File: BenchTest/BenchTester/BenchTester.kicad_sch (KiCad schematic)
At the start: 20 parts, among them J1 Conn_01x01_Socket, J2 Conn_01x01_Socket, J3 Conn_01x01_Socket, J5 Conn_01x01_Socket, J6 Conn_01x01_Socket, J7 Conn_01x01_Socket, J8 Conn_01x01_Socket, J9 Conn_01x01_Socket, Q1 Q_NMOS_Depletion_DGS, Q2 Q_NMOS_Depletion_DGS, Q3 Q_NMOS_Depletion_DGS, Q4 Q_NMOS_Depletion_DGS

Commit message: WIP for Zenn motor controller
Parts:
- added D1, D2, D3, D4: D_KAA, symbol Device:D_KAA
- added H1, H2, H3, H4: MountingHole, MountingHole:MountingHole_5.3mm_M5, symbol Mechanical:MountingHole
- added J4: Conn_01x02_Socket, Connector_PinHeader_2.54mm:PinHeader_1x02_P2.54mm_Vertical, symbol Connector:Conn_01x02_Socket
- R1, R3, R7, R8: value R -> 100k; footprint (none) -> Resistor_SMD:R_0402_1005Metric
- R2, R4, R5, R6: footprint (none) -> Resistor_SMD:R_0402_1005Metric
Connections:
- net DBUS: now also D1.1 (K), D4.1 (K)
- net GND: now also J4.2 (Pin_2)
- net Motor0: now also D1.2 (A), D1.3 (A), D2.1 (K)
- net Motor1: now also D3.1 (K), D4.2 (A), D4.3 (A)
- net SBUS: now also D2.2 (A), D2.3 (A), D3.2 (A), D3.3 (A)
- net Vdrive: now also J4.1 (Pin_1)

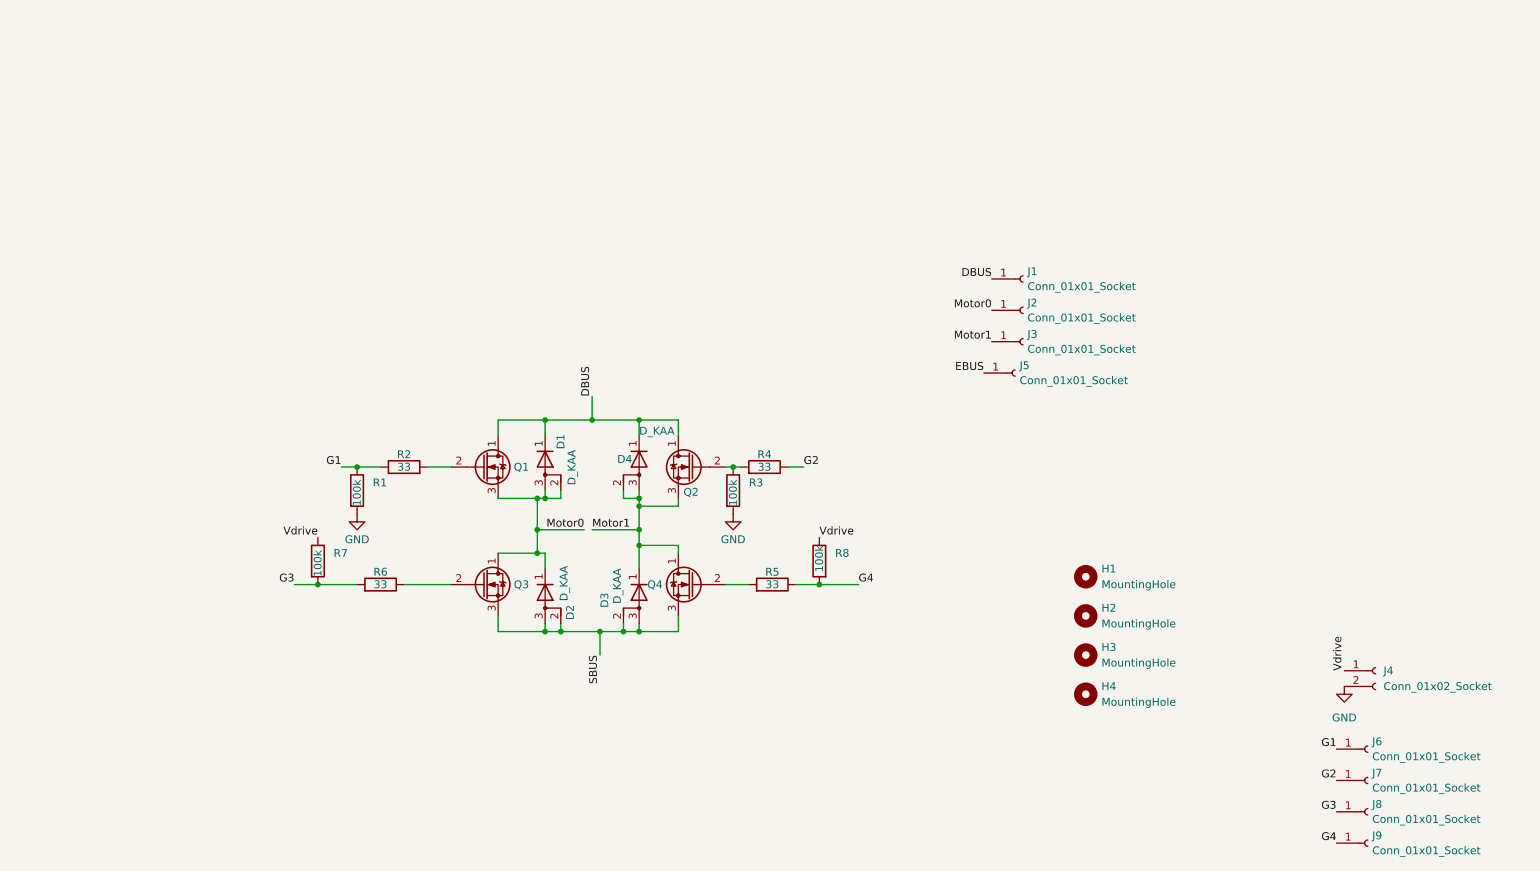
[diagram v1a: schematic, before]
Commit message: WIP - Diode / major parts assignment.
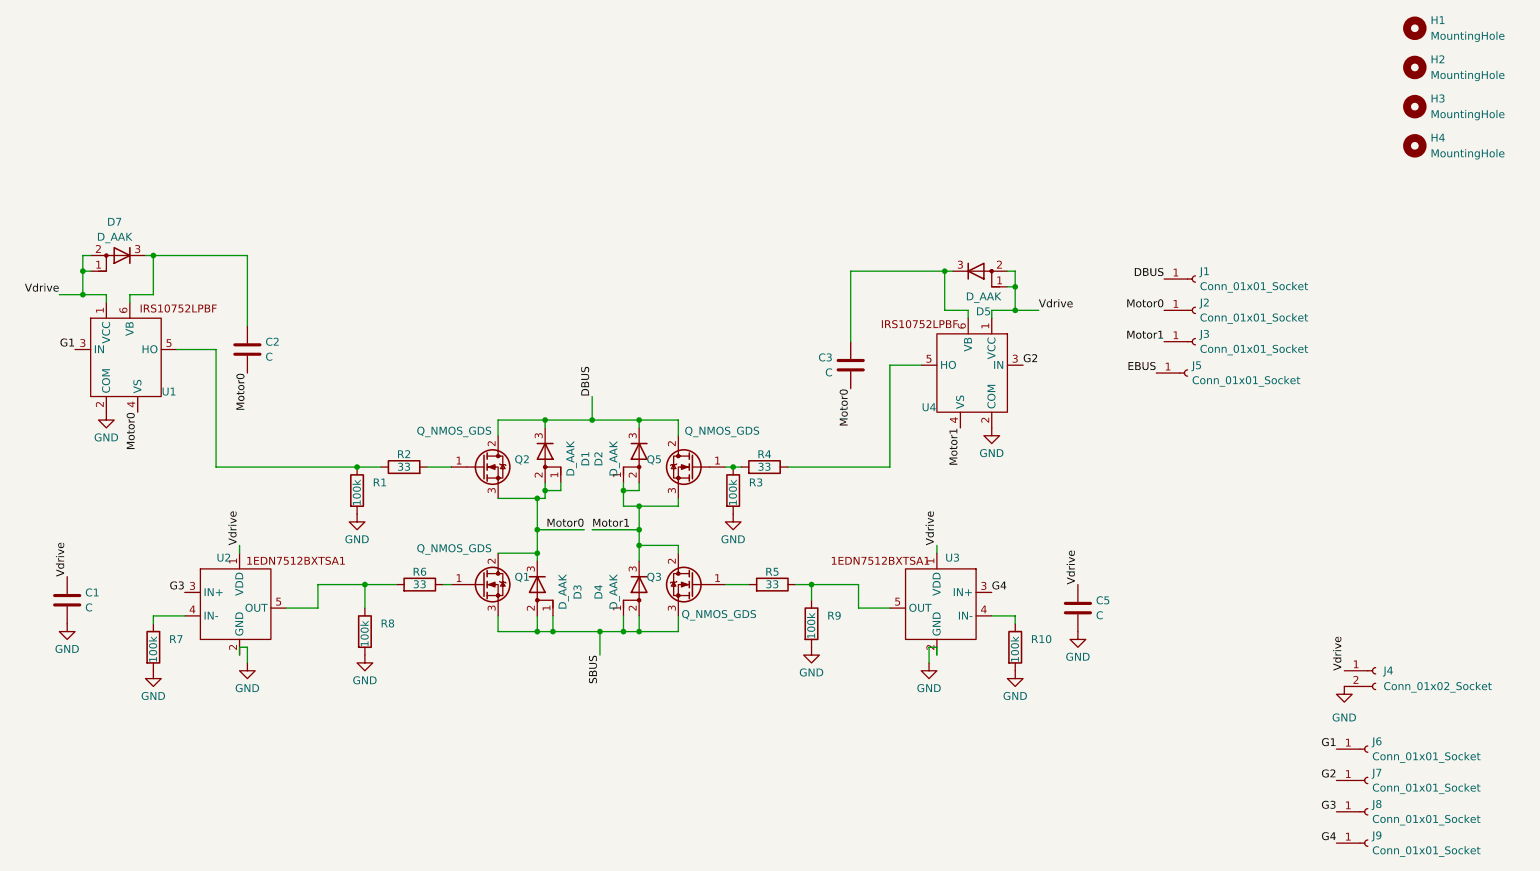
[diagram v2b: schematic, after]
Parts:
- removed D1, D2, D3, D4: D_KAA, symbol Device:D_KAA
- removed Q1, Q2, Q3, Q4: Q_NMOS_Depletion_DGS, symbol Device:Q_NMOS_Depletion_DGS
- added C1, C2, C3, C5: C, Capacitor_SMD:C_0805_2012Metric, symbol Device:C
- added D1, D2, D3, D4, D5, D7: D_AAK, Library:TO-252-2_SBR20M150D1Q, symbol Device:D_AAK
- added Q1, Q2, Q3, Q5: Q_NMOS_GDS, Package_TO_SOT_THT:TO-220-3_Vertical, symbol Device:Q_NMOS_GDS
- added R10, R9: 100k, Resistor_SMD:R_0402_1005Metric, symbol Device:R
- added U1, U4: ~, Package_TO_SOT_SMD:SOT-23-6_Handsoldering, symbol New_Library:IRS10752LPBF
- added U2, U3: ~, Package_TO_SOT_SMD:SC-74A-5_1.55x2.9mm_P0.95mm, symbol New_Library:1EDN7512BXTSA1
- H1, H2, H3: footprint MountingHole:MountingHole_5.3mm_M5 -> MountingHole:MountingHole_3.2mm_M3
- H4: footprint MountingHole:MountingHole_5.3mm_M5 -> MountingHole:MountingHole_3.2mm_M3_Pad
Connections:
- net DBUS: now also D1.3 (K), D2.3 (K), Q2.2 (D), Q5.2 (D)
- net G1: now also U1.3 (IN); no longer R1.1, R2.1
- net G2: now also U4.3 (IN); no longer R4.1
- net G3: now also U2.3 (IN+); no longer R6.2, R7.2
- net G4: now also U3.3 (IN+); no longer R5.1, R8.2
- net GND: now also R7.2, R8.2, C1.2, C5.2, R10.2, R9.2, U1.2 (COM), U2.2 (GND), U3.2 (GND), U4.2 (COM)
- net Motor0: now also C2.2, C3.2, D1.1 (A), D1.2 (A), D3.3 (K), Q1.2 (D), Q2.3 (S), U1.4 (VS)
- net Motor1: now also D2.1 (A), D2.2 (A), D4.3 (K), Q3.2 (D), Q5.3 (S), U4.4 (VS)
- net SBUS: now also D3.1 (A), D3.2 (A), D4.1 (A), D4.2 (A), Q1.3 (S), Q3.3 (S)
- net Vdrive: now also C1.1, C5.1, D5.1 (A), D5.2 (A), D7.1 (A), D7.2 (A), U1.1 (VCC), U2.1 (VDD), U3.1 (VDD), U4.1 (VCC); no longer R7.1, R8.1
- net at R2.2: now also Q2.1 (G)
- net at R3.1, R4.2: now also Q5.1 (G)
- net at R6.1: now also Q1.1 (G)
- net at R5.2: now also Q3.1 (G)
- new net: R6.2, R8.1, U2.5 (OUT)
- new net: R1.1, R2.1, U1.5 (HO)
- new net: C2.1, D7.3 (K), U1.6 (VB)
- new net: C3.1, D5.3 (K), U4.6 (VB)
- new net: R4.1, U4.5 (HO)
- new net: R10.1, U3.4 (IN-)
- new net: R5.1, R9.1, U3.5 (OUT)
- new net: R7.1, U2.4 (IN-)
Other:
- moved on the sheet: H1, H2, H3, H4, J1, J2, J3, J5, R6

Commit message: Initial Placement
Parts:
- H4: footprint MountingHole:MountingHole_3.2mm_M3_Pad -> MountingHole:MountingHole_3.2mm_M3
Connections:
- net EBUS is gone; now on net SBUS: J5.1 (Pin_1)
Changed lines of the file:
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@@
 	(label "Motor0"
 		(at 71.12 72.39 270)
-		(fields_autoplaced yes)
 		(effects
 			(font
@@
 	(label "G4"
 		(at 191.77 107.95 0)
-		(fields_autoplaced yes)
 		(effects
 			(font
@@
 	(label "DBUS"
 		(at 219.71 57.15 180)
-		(fields_autoplaced yes)
 		(effects
 			(font
@@
 	(label "Motor0"
 		(at 125.73 97.79 180)
-		(fields_autoplaced yes)
 		(effects
 			(font
@@
 	(label "Vdrive"
 		(at 69.85 100.33 90)
-		(fields_autoplaced yes)
 		(effects
 			(font
@@
 	(label "G1"
 		(at 43.18 68.58 180)
-		(fields_autoplaced yes)
 		(effects
 			(font
@@
 	(label "G2"
 		(at 247.65 138.43 180)
-		(fields_autoplaced yes)
 		(effects
 			(font
@@
 	(label "DBUS"
 		(at 127 76.2 90)
-		(fields_autoplaced yes)
 		(effects
 			(font
@@
 	(label "Motor1"
 		(at 127 97.79 0)
-		(fields_autoplaced yes)
 		(effects
 			(font
@@
 	(label "Motor0"
 		(at 168.91 74.93 270)
-		(fields_autoplaced yes)
 		(effects
 			(font
@@
 		)
 	)
-	(label "EBUS"
+	(label "SBUS"
 		(at 218.44 72.39 180)
-		(fields_autoplaced yes)
 		(effects
 			(font
@@
 	(label "Vdrive"
 		(at 248.92 120.65 90)
-		(fields_autoplaced yes)
 		(effects
 			(font
@@
 	(label "Vdrive"
 		(at 40.64 59.69 180)
-		(fields_autoplaced yes)
 		(effects
 			(font
@@
 	(label "Motor0"
 		(at 219.71 62.23 180)
-		(fields_autoplaced yes)
 		(effects
 			(font
@@
 	(label "SBUS"
 		(at 128.27 118.11 270)
-		(fields_autoplaced yes)
 		(effects
 			(font
@@
 	(label "Motor1"
 		(at 186.69 81.28 270)
-		(fields_autoplaced yes)
 		(effects
 			(font
@@
 	(label "G3"
 		(at 60.96 107.95 180)
-		(fields_autoplaced yes)
 		(effects
 			(font
@@
 	(label "G2"
 		(at 196.85 71.12 0)
-		(fields_autoplaced yes)
 		(effects
 			(font
@@
 	(label "Vdrive"
 		(at 205.74 106.68 90)
-		(fields_autoplaced yes)
 		(effects
 			(font
@@
 	(label "Motor0"
 		(at 53.34 78.74 270)
-		(fields_autoplaced yes)
 		(effects
 			(font
@@
 	(label "Vdrive"
 		(at 41.91 105.41 90)
-		(fields_autoplaced yes)
 		(effects
 			(font
@@
 	(label "Vdrive"
 		(at 199.39 62.23 0)
-		(fields_autoplaced yes)
 		(effects
 			(font
@@
 	(label "G4"
 		(at 247.65 148.59 180)
-		(fields_autoplaced yes)
 		(effects
 			(font
@@
 	(label "G1"
 		(at 247.65 133.35 180)
-		(fields_autoplaced yes)
 		(effects
 			(font
@@
 	(label "G3"
 		(at 247.65 143.51 180)
-		(fields_autoplaced yes)
 		(effects
 			(font
@@
 	(label "Vdrive"
 		(at 182.88 100.33 90)
-		(fields_autoplaced yes)
 		(effects
 			(font
@@
 	(label "Motor1"
 		(at 219.71 67.31 180)
-		(fields_autoplaced yes)
 		(effects
 			(font
@@
 			)
 		)
-		(property "Footprint" "MountingHole:MountingHole_3.2mm_M3_Pad"
+		(property "Footprint" "MountingHole:MountingHole_3.2mm_M3"
 			(at 260.35 35.56 0)
 			(effects

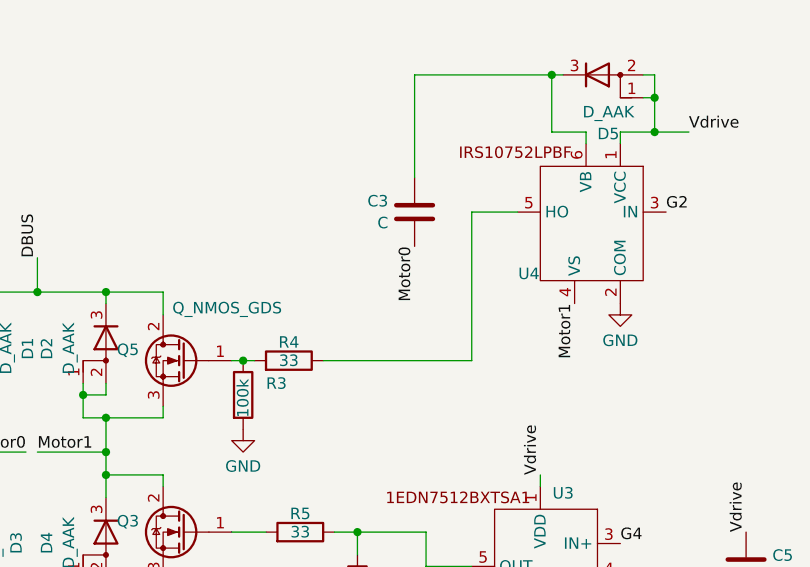
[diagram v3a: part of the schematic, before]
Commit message: Grouping Near Complete
Grouping of components is close to complete. Next is placement near
respective other groups. Need Full Footprint for FET with heatsink
before completing that exercise.
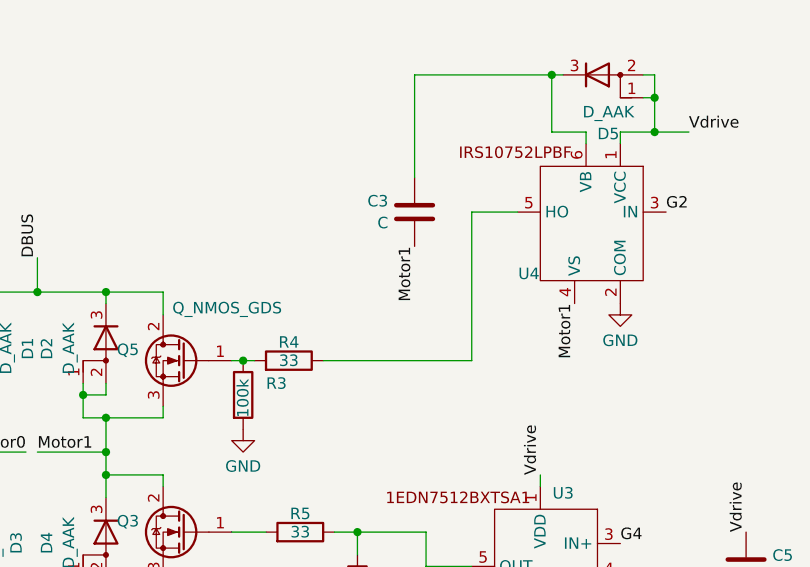
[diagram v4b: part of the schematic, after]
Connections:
- net Motor0: no longer C3.2
- net Motor1: now also C3.2
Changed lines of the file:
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@@
 		)
 	)
-	(label "Motor0"
+	(label "Motor1"
 		(at 168.91 74.93 270)
 		(effects

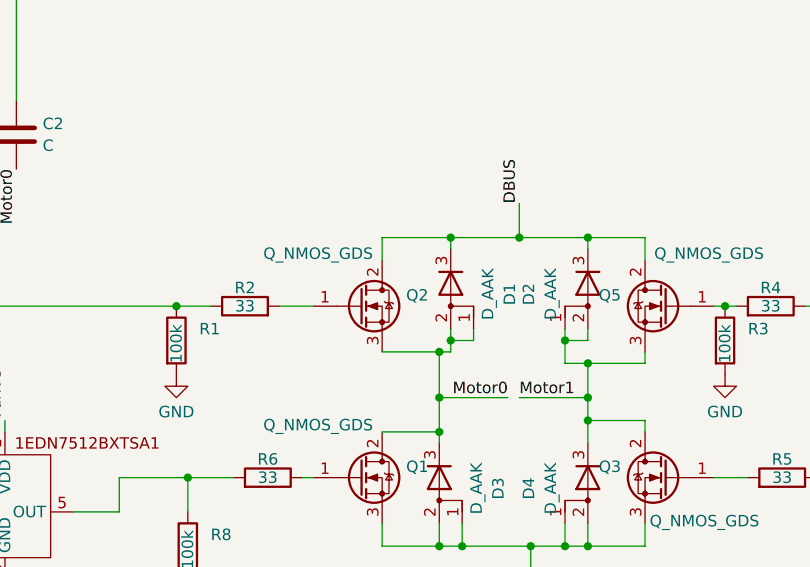
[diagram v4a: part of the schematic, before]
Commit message: Footprint assignment
Footprint assignment for Fets.
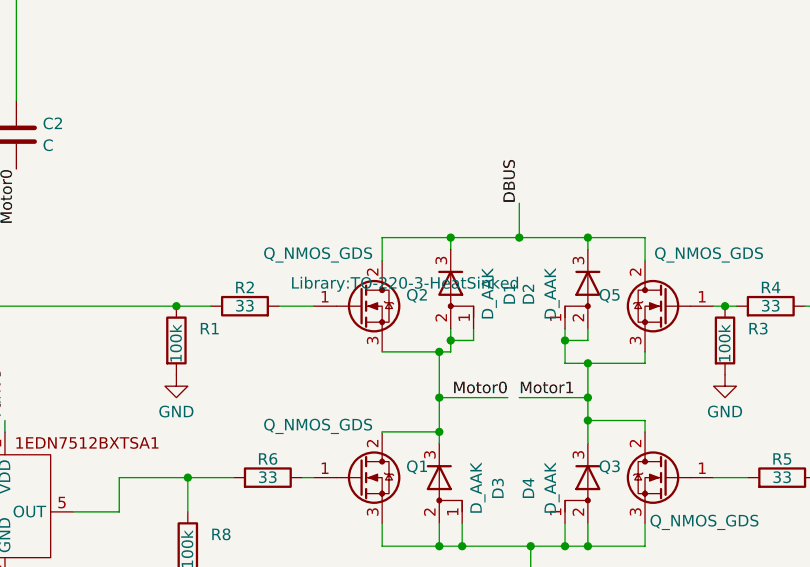
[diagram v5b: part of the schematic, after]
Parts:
- Q1, Q2, Q3, Q5: footprint Package_TO_SOT_THT:TO-220-3_Vertical -> Library:TO-220-3-HeatSinked
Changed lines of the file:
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@@
 	(label "Motor0"
 		(at 71.12 72.39 270)
+		(fields_autoplaced yes)
 		(effects
 			(font
@@
 	(label "G4"
 		(at 191.77 107.95 0)
+		(fields_autoplaced yes)
 		(effects
 			(font
@@
 	(label "DBUS"
 		(at 219.71 57.15 180)
+		(fields_autoplaced yes)
 		(effects
 			(font
@@
 	(label "Motor0"
 		(at 125.73 97.79 180)
+		(fields_autoplaced yes)
 		(effects
 			(font
@@
 	(label "Vdrive"
 		(at 69.85 100.33 90)
+		(fields_autoplaced yes)
 		(effects
 			(font
@@
 	(label "G1"
 		(at 43.18 68.58 180)
+		(fields_autoplaced yes)
 		(effects
 			(font
@@
 	(label "G2"
 		(at 247.65 138.43 180)
+		(fields_autoplaced yes)
 		(effects
 			(font
@@
 	(label "DBUS"
 		(at 127 76.2 90)
+		(fields_autoplaced yes)
 		(effects
 			(font
@@
 	(label "Motor1"
 		(at 127 97.79 0)
+		(fields_autoplaced yes)
 		(effects
 			(font
@@
 	(label "Motor1"
 		(at 168.91 74.93 270)
+		(fields_autoplaced yes)
 		(effects
 			(font
@@
 	(label "SBUS"
 		(at 218.44 72.39 180)
+		(fields_autoplaced yes)
 		(effects
 			(font
@@
 	(label "Vdrive"
 		(at 248.92 120.65 90)
+		(fields_autoplaced yes)
 		(effects
 			(font
@@
 	(label "Vdrive"
 		(at 40.64 59.69 180)
+		(fields_autoplaced yes)
 		(effects
 			(font
@@
 	(label "Motor0"
 		(at 219.71 62.23 180)
+		(fields_autoplaced yes)
 		(effects
 			(font
@@
 	(label "SBUS"
 		(at 128.27 118.11 270)
+		(fields_autoplaced yes)
 		(effects
 			(font
@@
 	(label "Motor1"
 		(at 186.69 81.28 270)
+		(fields_autoplaced yes)
 		(effects
 			(font
@@
 	(label "G3"
 		(at 60.96 107.95 180)
+		(fields_autoplaced yes)
 		(effects
 			(font
@@
 	(label "G2"
 		(at 196.85 71.12 0)
+		(fields_autoplaced yes)
 		(effects
 			(font
@@
 	(label "Vdrive"
 		(at 205.74 106.68 90)
+		(fields_autoplaced yes)
 		(effects
 			(font
@@
 	(label "Motor0"
 		(at 53.34 78.74 270)
+		(fields_autoplaced yes)
 		(effects
 			(font
@@
 	(label "Vdrive"
 		(at 41.91 105.41 90)
+		(fields_autoplaced yes)
 		(effects
 			(font
@@
 	(label "Vdrive"
 		(at 199.39 62.23 0)
+		(fields_autoplaced yes)
 		(effects
 			(font
@@
 	(label "G4"
 		(at 247.65 148.59 180)
+		(fields_autoplaced yes)
 		(effects
 			(font
@@
 	(label "G1"
 		(at 247.65 133.35 180)
+		(fields_autoplaced yes)
 		(effects
 			(font
@@
 	(label "G3"
 		(at 247.65 143.51 180)
+		(fields_autoplaced yes)
 		(effects
 			(font
@@
 	(label "Vdrive"
 		(at 182.88 100.33 90)
+		(fields_autoplaced yes)
 		(effects
 			(font
@@
 	(label "Motor1"
 		(at 219.71 67.31 180)
+		(fields_autoplaced yes)
 		(effects
 			(font
@@
 			)
 		)
-		(property "Footprint" "Package_TO_SOT_THT:TO-220-3_Vertical"
+		(property "Footprint" "Library:TO-220-3-HeatSinked"
 			(at 138.43 104.14 0)
 			(effects
@@
 			)
 		)
-		(property "Footprint" "Package_TO_SOT_THT:TO-220-3_Vertical"
+		(property "Footprint" "Library:TO-220-3-HeatSinked"
 			(at 138.43 85.09 0)
 			(effects
@@
 			)
 		)
-		(property "Footprint" "Package_TO_SOT_THT:TO-220-3_Vertical"
+		(property "Footprint" "Library:TO-220-3-HeatSinked"
 			(at 114.3 104.14 0)
 			(effects
@@
 			)
 		)
-		(property "Footprint" "Package_TO_SOT_THT:TO-220-3_Vertical"
+		(property "Footprint" "Library:TO-220-3-HeatSinked"
 			(at 114.3 85.09 0)
 			(effects
@@
 					(size 1.27 1.27)
 				)
-				(hide yes)
 			)
 		)
